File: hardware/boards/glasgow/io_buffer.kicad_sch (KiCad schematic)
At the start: 68 parts, among them J2 IDC-Header_2x10_P2.54mm, J8 Conn_01x08, J9 Conn_01x08, U10 SN74LVC1T45DCKR, U11 SN74LVC1T45DCKR, U16 SN74LVC1T45DCKR, U17 SN74LVC1T45DCKR, U18 SN74LVC1T45DCKR, U19 PCA6408APW, U20 DAC081C081CIMK, U21 INA233, U31 TPS73101DBV, U4 SN74LVC1T45DCKR, U6 SN74LVC1T45DCKR, U9 SN74LVC1T45DCKR

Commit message: revC3: Increased min pad gap to 0.22mm.
This increases the chances of getting solder mask bridges between pads
decreasing probability of bridging.
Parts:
- U21: footprint Package_SO:VSSOP-10_3x3mm_P0.5mm -> Glasgow:VSSOP-10_3x3mm_P0.5mm
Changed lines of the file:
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@@
     (property "Reference" "U21" (id 0) (at 255.27 63.5 0))
     (property "Value" "INA233" (id 1) (at 267.97 63.5 0))
-    (property "Footprint" "Package_SO:VSSOP-10_3x3mm_P0.5mm" (id 2) (at 281.94 86.36 0)
+    (property "Footprint" "Glasgow:VSSOP-10_3x3mm_P0.5mm" (id 2) (at 281.94 86.36 0)
       (effects (font (size 1.27 1.27)) hide)
     )

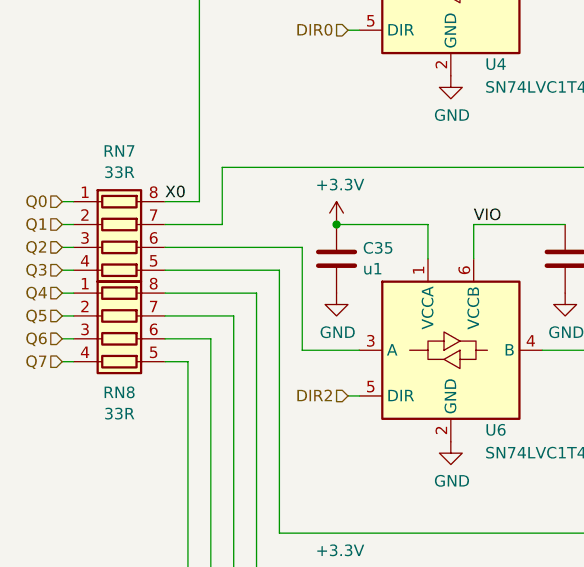
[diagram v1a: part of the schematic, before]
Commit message: revC3: Final cleanups before production.
* Changed 3D models to step so the 3D model can be exported for
  enclosure CAD.
* Changed silk and stop colors to match 1BitSquared production boards
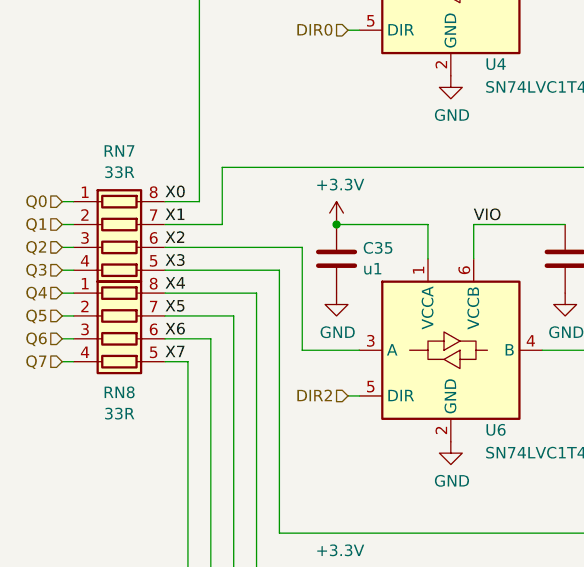
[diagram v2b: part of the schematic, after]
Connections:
- net X2: now reaches RN7.6 (R3.2), U6.3 (A)
- net X4: now reaches RN8.8 (R1.2), U9.3 (A)
- net X6: now reaches RN8.6 (R3.2), U10.3 (A)
- net X1: now reaches RN7.7 (R2.2), U11.3 (A)
- net X3: now reaches RN7.5 (R4.2), U16.3 (A)
- net X5: now reaches RN8.7 (R2.2), U17.3 (A)
- net X7: now reaches RN8.5 (R4.2), U18.3 (A)

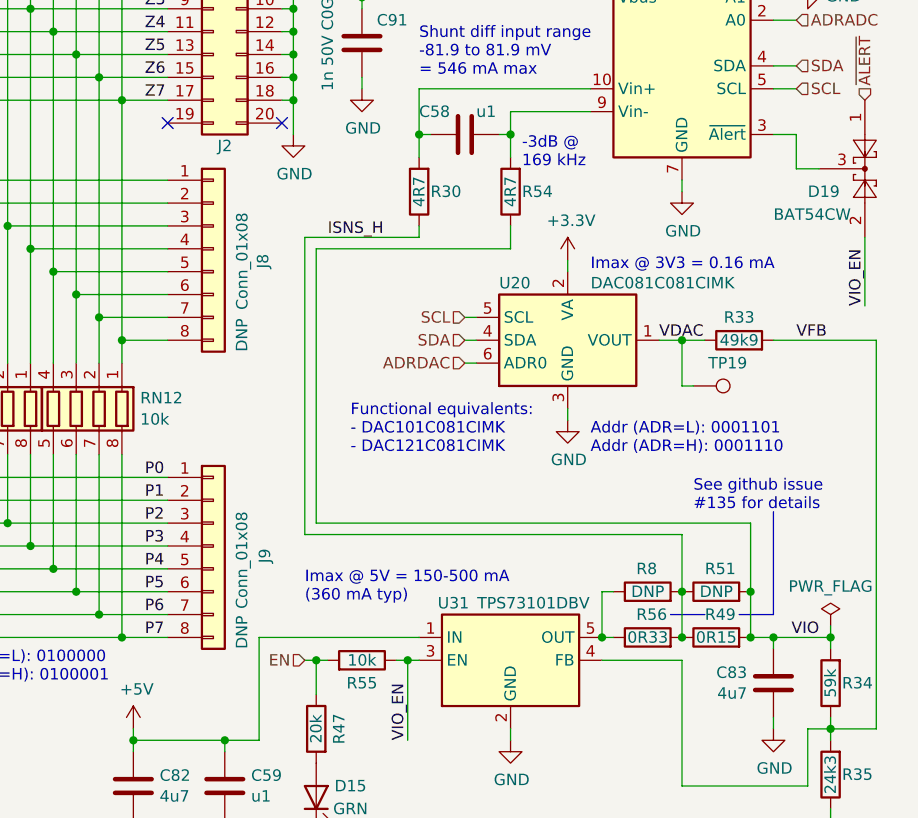
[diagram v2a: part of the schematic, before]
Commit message: revC3: Use the new KiCad DNP flag for the DNP parts.
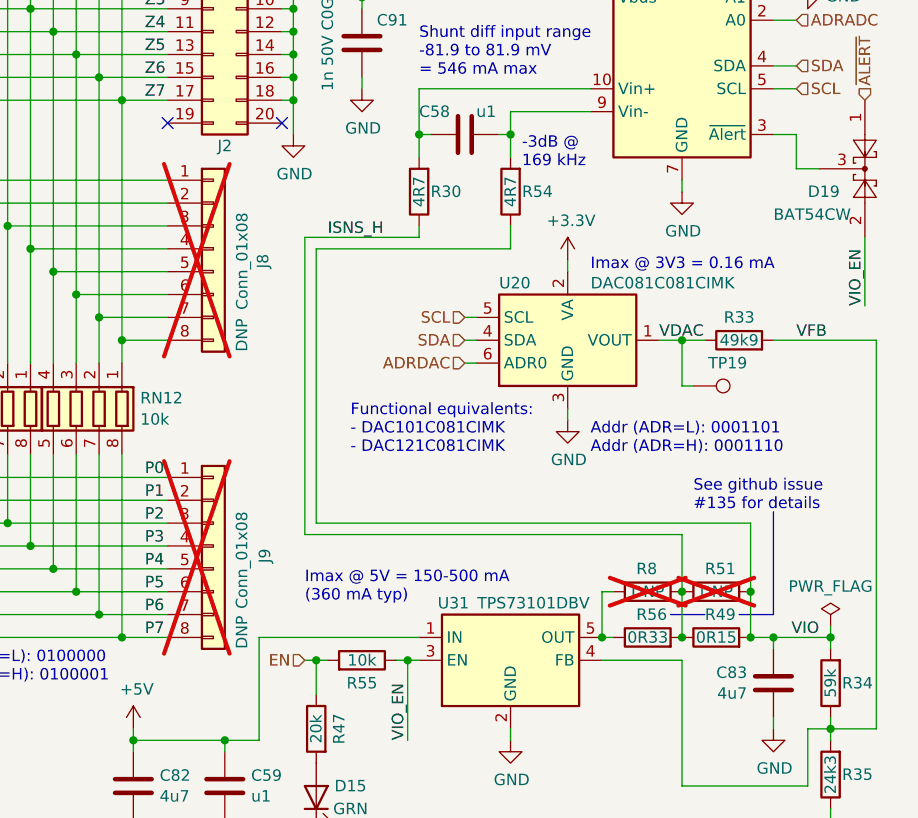
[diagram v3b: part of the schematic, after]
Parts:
- J8, J9, R51, R8: now not fitted; now left out of the parts list
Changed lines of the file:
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@@
   )
   (symbol (lib_id "Device:R") (at 265.43 133.35 90) (unit 1)
-    (in_bom yes) (on_board yes) (dnp no)
+    (in_bom no) (on_board yes) (dnp yes)
     (property "Reference" "R51" (at 264.16 130.81 90)
       (effects (font (size 1.27 1.27)) (justify right))
@@
   )
   (symbol (lib_id "Connector_Generic:Conn_01x08") (at 209.55 95.25 0) (unit 1)
-    (in_bom yes) (on_board yes) (dnp no)
+    (in_bom no) (on_board yes) (dnp yes)
     (property "Reference" "J8" (at 215.0618 96.6216 90)
       (effects (font (size 1.27 1.27)))
@@
   )
   (symbol (lib_id "Connector_Generic:Conn_01x08") (at 209.55 128.27 0) (unit 1)
-    (in_bom yes) (on_board yes) (dnp no)
+    (in_bom no) (on_board yes) (dnp yes)
     (property "Reference" "J9" (at 215.265 130.175 90)
       (effects (font (size 1.27 1.27)) (justify left))
@@
   )
   (symbol (lib_id "Device:R") (at 257.81 133.35 90) (unit 1)
-    (in_bom yes) (on_board yes) (dnp no)
+    (in_bom no) (on_board yes) (dnp yes)
     (property "Reference" "R8" (at 256.54 130.81 90)
       (effects (font (size 1.27 1.27)) (justify right))

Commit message: revC3: Marked non schematic/bom parts correctly.
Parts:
- J8, J9, R51, R8: now in the parts list
- TP19: now left out of the parts list
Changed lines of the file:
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@@
   )
   (symbol (lib_id "Device:R") (at 265.43 133.35 90) (unit 1)
-    (in_bom no) (on_board yes) (dnp yes)
+    (in_bom yes) (on_board yes) (dnp yes)
     (property "Reference" "R51" (at 264.16 130.81 90)
       (effects (font (size 1.27 1.27)) (justify right))
@@
   )
   (symbol (lib_id "Connector:TestPoint") (at 262.89 110.49 270) (unit 1)
-    (in_bom yes) (on_board yes) (dnp no)
+    (in_bom no) (on_board yes) (dnp no)
     (property "Reference" "TP19" (at 266.7 107.95 90)
       (effects (font (size 1.27 1.27)))
@@
   )
   (symbol (lib_id "Connector_Generic:Conn_01x08") (at 209.55 95.25 0) (unit 1)
-    (in_bom no) (on_board yes) (dnp yes)
+    (in_bom yes) (on_board yes) (dnp yes)
     (property "Reference" "J8" (at 215.0618 96.6216 90)
       (effects (font (size 1.27 1.27)))
@@
   )
   (symbol (lib_id "Connector_Generic:Conn_01x08") (at 209.55 128.27 0) (unit 1)
-    (in_bom no) (on_board yes) (dnp yes)
+    (in_bom yes) (on_board yes) (dnp yes)
     (property "Reference" "J9" (at 215.265 130.175 90)
       (effects (font (size 1.27 1.27)) (justify left))
@@
   )
   (symbol (lib_id "Device:R") (at 257.81 133.35 90) (unit 1)
-    (in_bom no) (on_board yes) (dnp yes)
+    (in_bom yes) (on_board yes) (dnp yes)
     (property "Reference" "R8" (at 256.54 130.81 90)
       (effects (font (size 1.27 1.27)) (justify right))

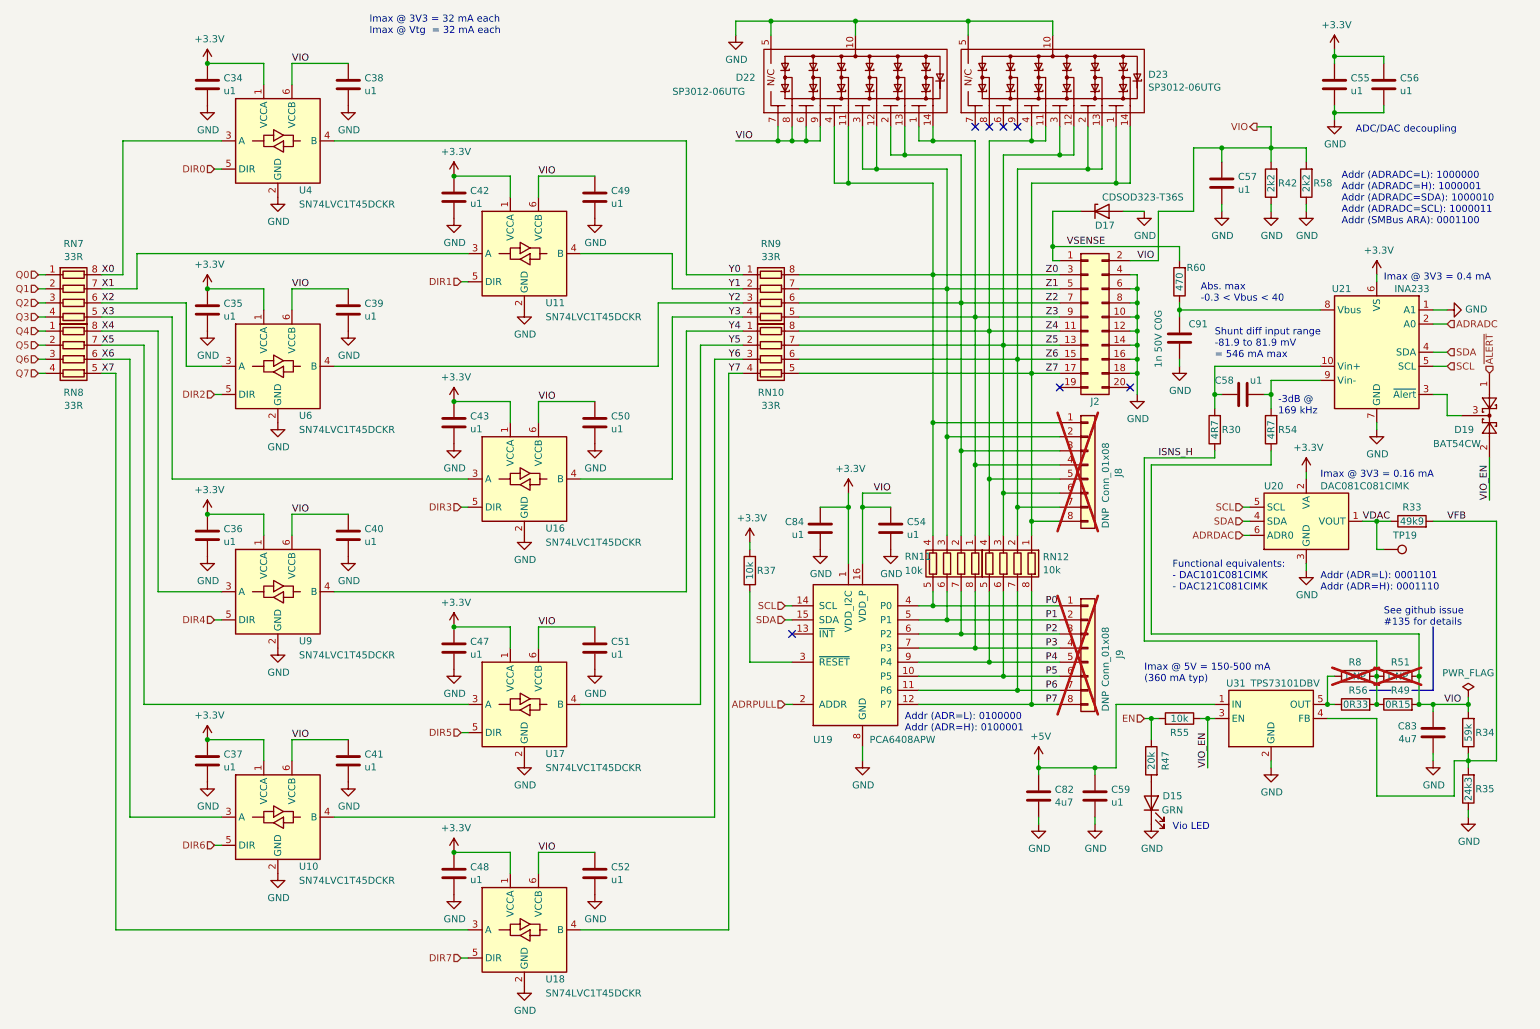
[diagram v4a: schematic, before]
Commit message: hardware: open & save with KiCAD 8.0.9
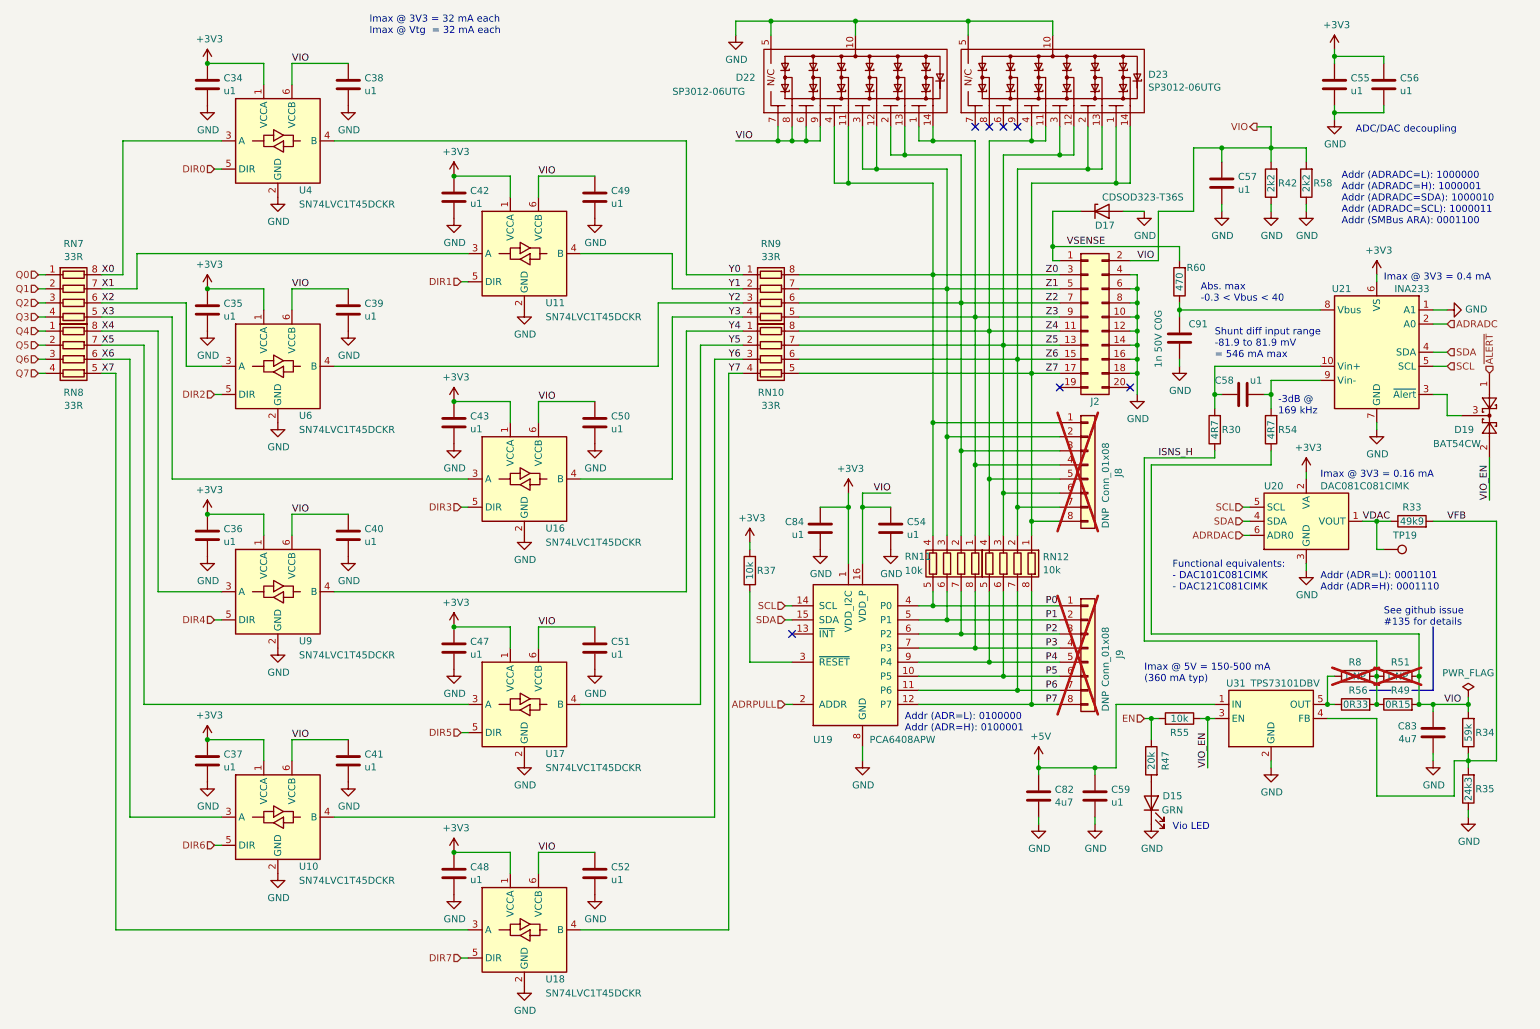
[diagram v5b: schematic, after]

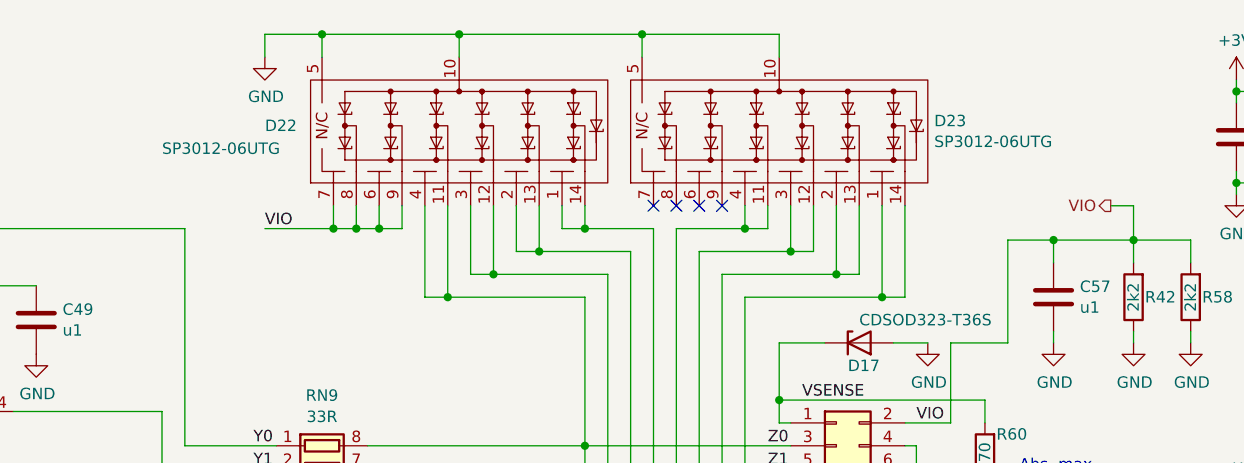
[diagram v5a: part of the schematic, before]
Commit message: hardware: change EOL SP3012-06UTG ESD diodes to SC7538-08UTG.
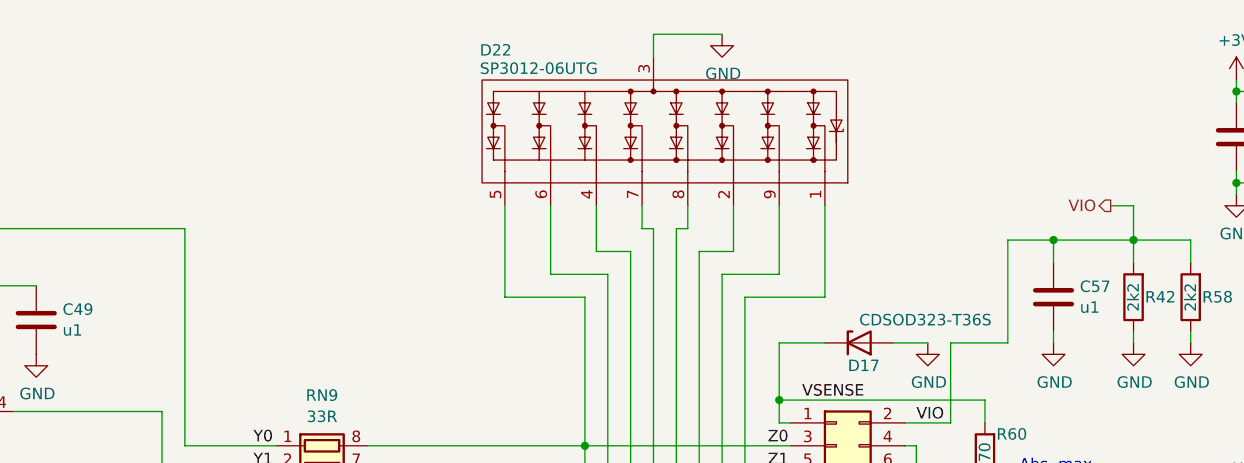
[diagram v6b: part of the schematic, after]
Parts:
- removed D23: SP3012-06UTG, Glasgow:UDFN-14_3.5x1.35mm_P0.5mm, symbol Glasgow:SP3012-06UTG
- D22: footprint Glasgow:UDFN-14_3.5x1.35mm_P0.5mm -> Package_DFN_QFN:UDFN-9_1.0x3.8mm_P0.5mm; symbol Glasgow:SP3012-06UTG -> Glasgow:SC7538-08UTG
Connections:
- net GND: now also D22.3 (GND); no longer D22.10 (GND), D22.5 (N/C)
- net VIO: no longer D22.6 (N/C), D22.7 (N/C), D22.8 (Ch6), D22.9 (Ch5)
- net Z0: now also D22.5 (Ch8); no longer D22.11 (Ch4), D22.4 (N/C)
- net Z1: now also D22.6 (Ch7); no longer D22.12 (Ch3), D22.3 (N/C)
- net Z2: now also D22.4 (Ch6); no longer D22.13 (Ch2), D22.2 (N/C)
- net Z3: now also D22.7 (Ch5); no longer D22.1 (N/C), D22.14 (Ch1)
- net Z4: now also D22.8 (Ch4)
- net Z5: now also D22.2 (Ch3)
- net Z6: now also D22.9 (Ch2)
- net Z7: now also D22.1 (Ch1)
- no-connect marks 7 -> 3
